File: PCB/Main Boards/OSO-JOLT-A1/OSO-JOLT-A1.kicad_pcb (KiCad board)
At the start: 2 copper layers, 28.3 x 28.5 mm, 34 parts, among them J1 OSO_SWD, J2 FH19C-9S-0.5SH_10_, Q1 Q_NMOS_GSD, U1 ATSAML22J18A-MUT, U4 MIC5365-3.3YC5-TR, X1 Crystal

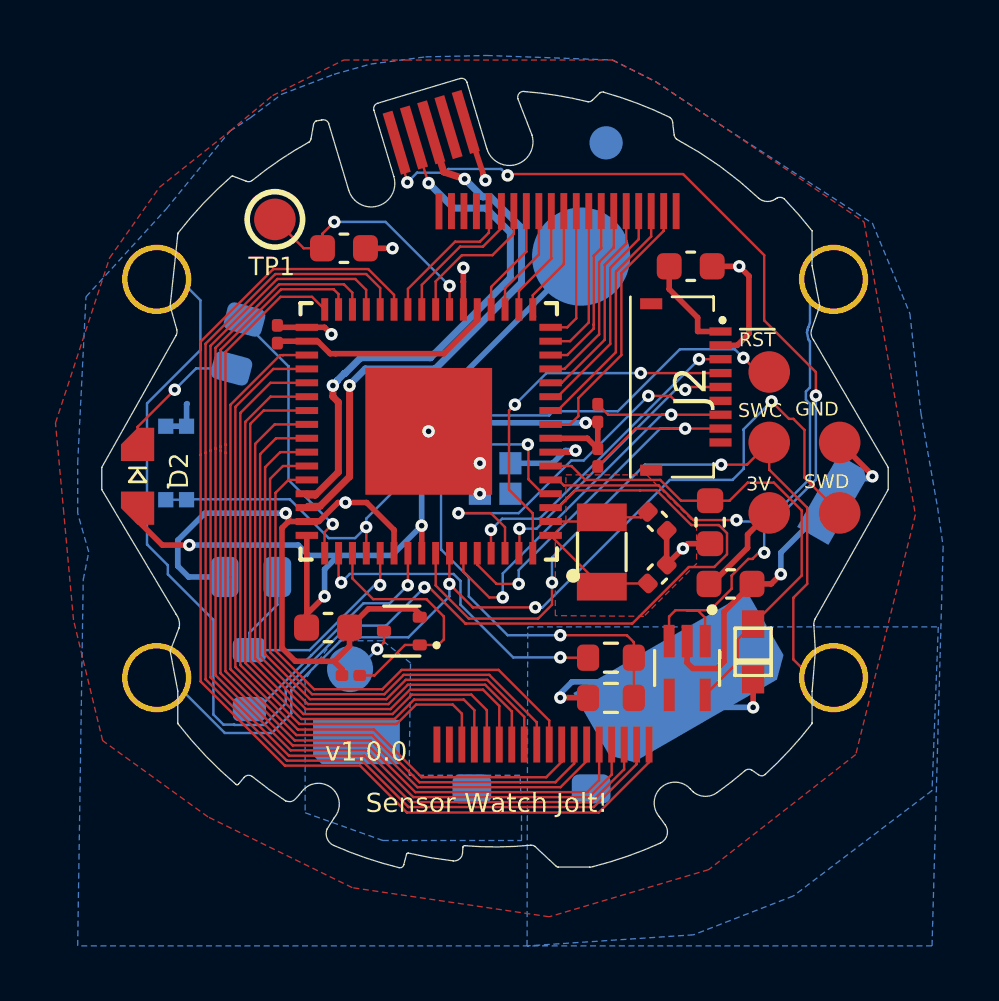
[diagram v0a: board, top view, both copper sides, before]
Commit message: Removed the daughterboard connector and placed LIS2DW directly on board
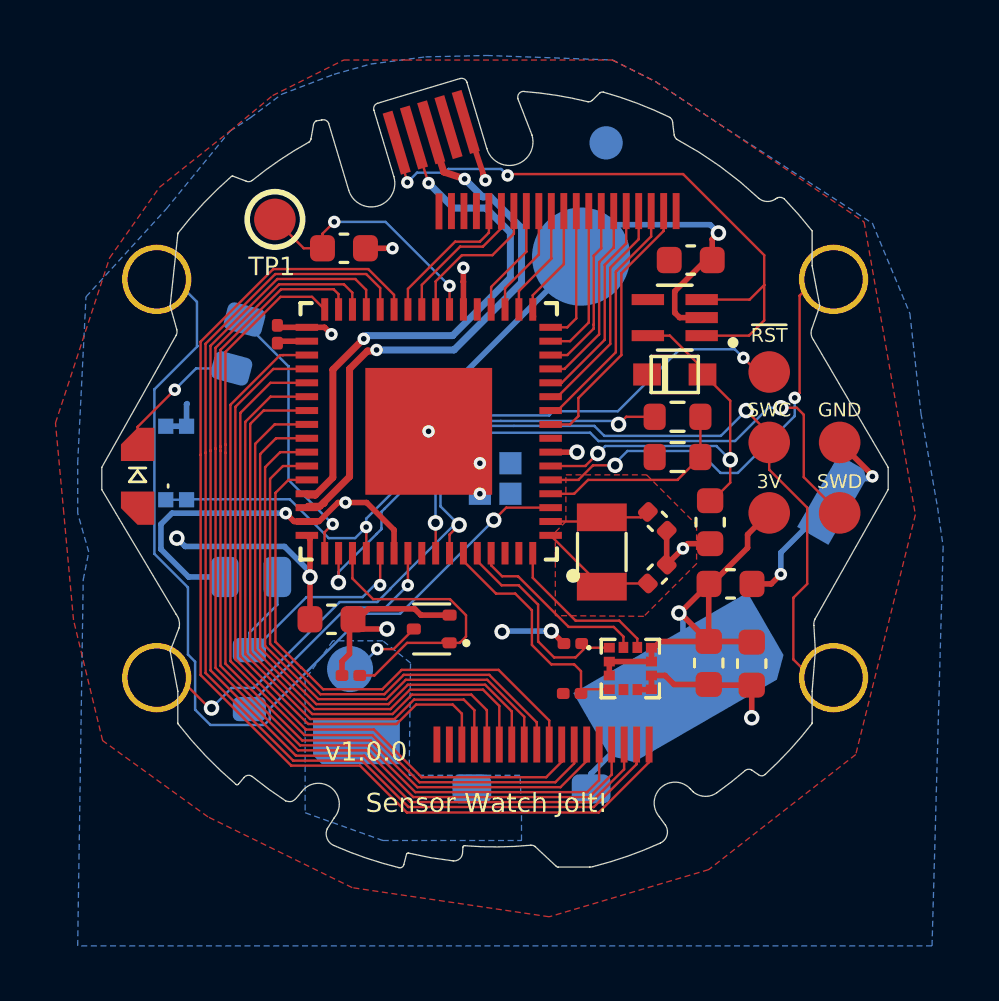
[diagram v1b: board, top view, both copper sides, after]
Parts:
- removed J2: FH19C-9S-0.5SH_10_, OSO-SWAT-A1-05:FH19C9S05SH10
- added C10: 10uF, Capacitor_SMD:C_0603_1608Metric, F.Cu at (166.3, 109.2)
- added C11: 0.1uF, Capacitor_SMD:C_0603_1608Metric, F.Cu at (164.8, 109.2)
- added U6: LIS2DW12TR, OSO-SWAT-A1-05:LGA12R50P4X4_200X200X70, F.Cu at (161.9, 109.4)
- moved U4 12.6 mm to (163.5, 96.8), turned to 180 degrees
- moved D1 10.4 mm to (163.5, 98.8), turned to 180 degrees
- moved R3 10.1 mm to (159.8, 110.3), turned to 0 degrees
- moved R6 9.01 mm to (163.6, 100.3)
- moved R5 9.01 mm to (163.6, 101.8)
- moved R4 6.77 mm to (159.8, 108.5), turned to 0 degrees
- moved Q1 1.08 mm to (154.8, 108.0)
- moved C4 0.32 mm to (151.2, 107.6)
- moved C2 0.23 mm to (164.1, 94.7)
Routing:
- net VCC: track 56.2 -> 34.8 mm, vias 6 -> 5
- net /ADJUST: track 48.6 -> 33.5 mm
- net /A1_SCK: track 14.1 -> 0.00 mm, vias 2 -> 0
- net /TEMPSENSE: track 19.6 -> 7.40 mm, vias 2 -> 0
- net VBUS: track 35.3 -> 23.2 mm, vias 4 -> 2
- net /A2_MOSI: track 10.3 -> 0.00 mm, vias 2 -> 0
- net /SCL: track 15.9 -> 7.73 mm, vias 2 -> 0
- net /A3/D0/CS: track 13.7 -> 5.88 mm, vias 2 -> 0
- net /SDA: track 16.4 -> 8.78 mm, vias 2 -> 0
- net /A4/D1/MISO: track 11.7 -> 6.66 mm, vias 2 -> 0
- net /~{TS_ENABLE}: track 11.9 -> 15.6 mm
- net +3V3: track 18.3 -> 15.0 mm, vias 0 -> 2
- net /START: track 17.8 -> 15.5 mm, vias 1 -> 2
- net /BUZZER: track 9.17 -> 10.8 mm
- net /BUZZER_HV: track 2.08 -> 2.95 mm
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- removed copper zone on B.Cu, net VCC

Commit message: This commit is what holds the design sent to JLCPCB
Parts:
- added Q2: Q_Photo_NPN, Resistor_SMD:R_0603_1608Metric, F.Cu at (158.1, 107.0)
- added R7: 20K, Resistor_SMD:R_0201_0603Metric, F.Cu at (157.7, 108.1)
- moved Q1 0.80 mm to (154.0, 107.9), turned to -90 degrees
- moved R1 0.33 mm to (151.8, 109.3)
- moved R6 0.10 mm to (163.6, 100.2)
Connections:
- U1 pad 62: /A1_SCK -> /LIGHTSENSE
- U1 pad 63: /A2_MOSI -> /~{LS_ENABLE}
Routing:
- net VCC: track 34.8 -> 40.1 mm
- net GND: track 67.0 -> 63.7 mm, vias 16 -> 17
- net /LIGHTSENSE: track 0.00 -> 2.94 mm
- net /A4/D1/MISO: track 6.66 -> 9.28 mm
- net /~{LS_ENABLE}: track 0.00 -> 2.16 mm
- net /BUZZER_HV: track 2.95 -> 1.06 mm
- net /SWCLK_LIGHT: track 26.4 -> 27.6 mm
- net /SEG20: track 21.2 -> 20.2 mm
- net /SEG18: track 21.9 -> 21.0 mm
- net /SEG19: track 21.7 -> 20.8 mm
- net /SEG21: track 20.7 -> 19.9 mm
- net /SEG17: track 22.2 -> 21.4 mm
- net /SEG23: track 19.2 -> 18.4 mm
- net /SDA: track 8.78 -> 9.55 mm
- net /SEG22: track 20.1 -> 19.4 mm
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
